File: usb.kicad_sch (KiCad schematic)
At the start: 46 parts, among them U10 CH397A, U11 XC6206PxxxMR, U3 XC6206PxxxMR, U4 CH343P, U6 CH334P, U9 CH343P, Y2 25MHz, Y3 12MHz

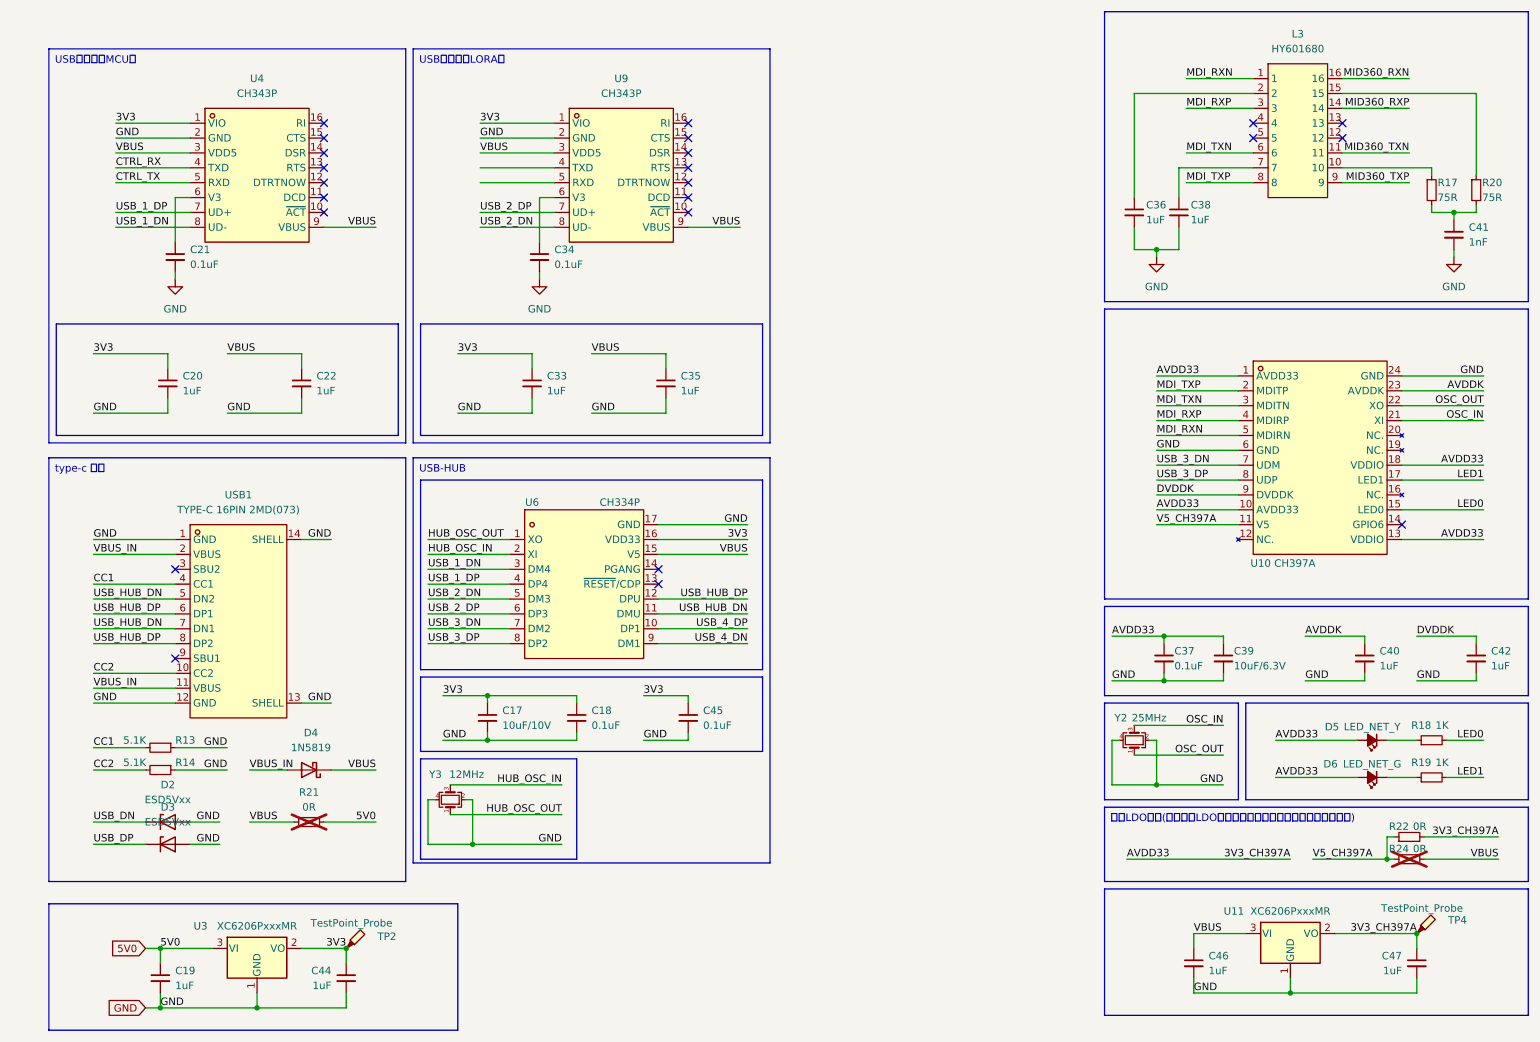
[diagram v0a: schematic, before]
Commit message: 暂存: 基本完成原理图(未分配封装，未ERC)
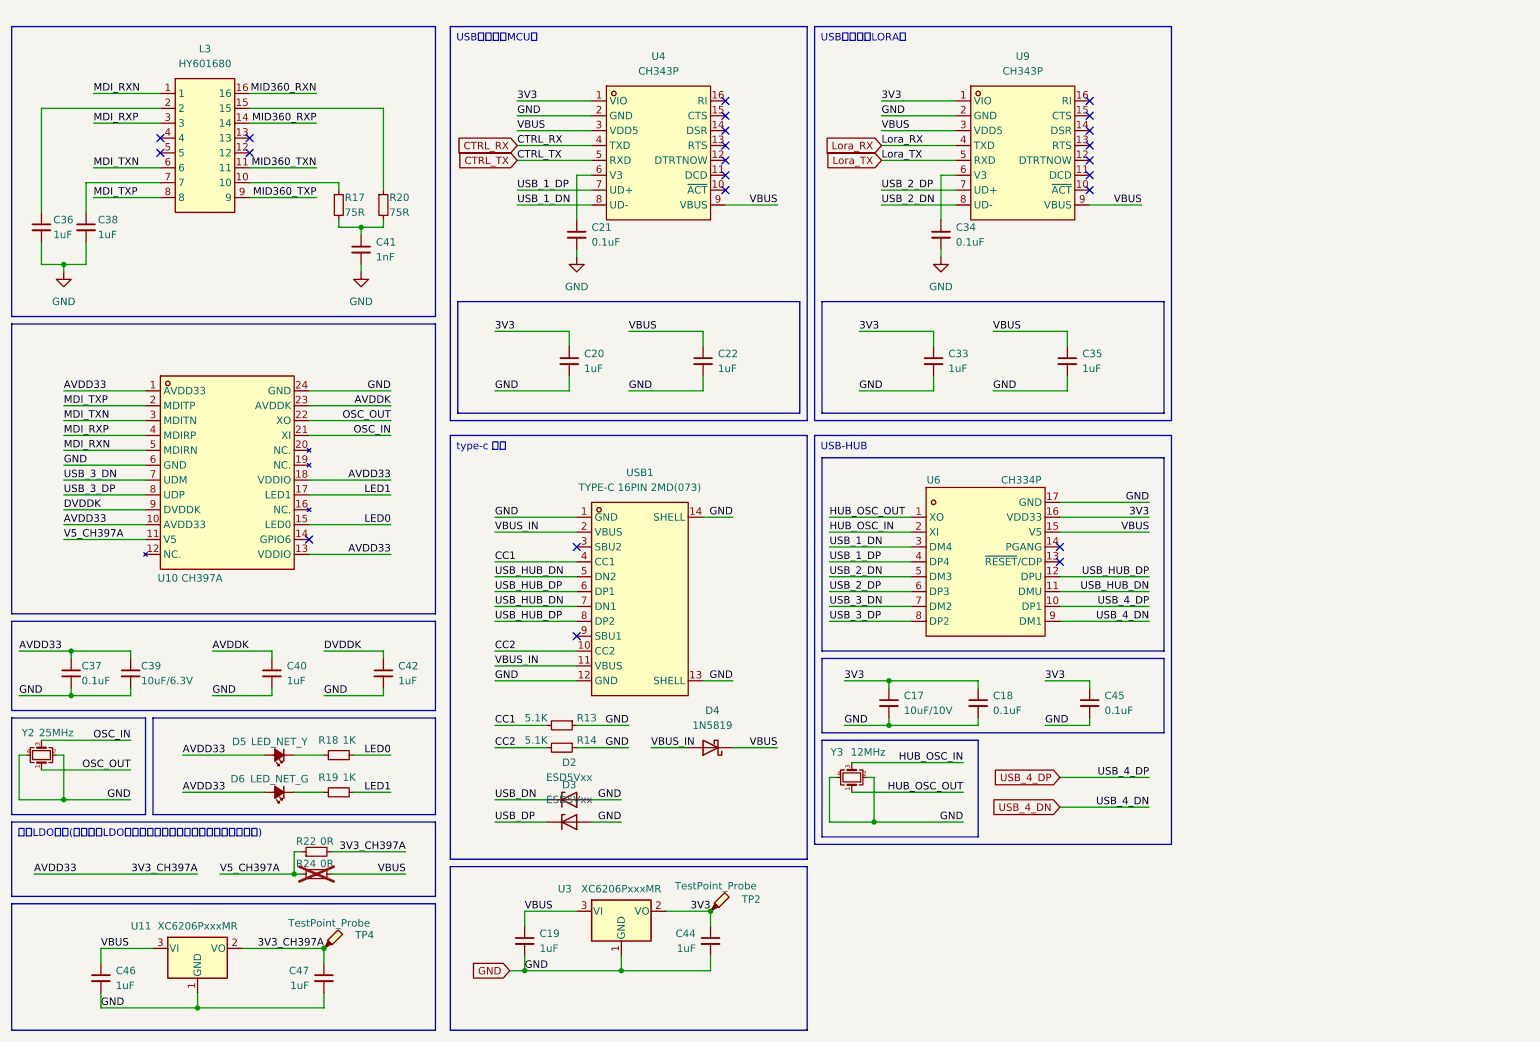
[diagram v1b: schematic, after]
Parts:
- removed R21: 0R, symbol Device:R_Small
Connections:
- net 5V0 is gone; now on net VBUS: C19.1, U3.3 (VI)
- net Lora_RX: now reaches U9.4 (TXD)
- net Lora_TX: now reaches U9.5 (RXD)
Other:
- moved on the sheet: C17, C18, C19, C20, C21, C22, C33, C34, C35, C36, C37, C38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

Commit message: 暂存: 基本完成原理图(差雷达接口)
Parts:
- C29: renamed from C36; footprint Capacitor_SMD:C_0603_1608Metric -> Capacitor_SMD:C_0402_1005Metric
- C32: renamed from C46; footprint Capacitor_SMD:C_0603_1608Metric -> Capacitor_SMD:C_0402_1005Metric
- C34: renamed from C40; footprint Capacitor_SMD:C_0603_1608Metric -> Capacitor_SMD:C_0402_1005Metric
- C35: renamed from C47; footprint Capacitor_SMD:C_0603_1608Metric -> Capacitor_SMD:C_0402_1005Metric
- C37: renamed from C42; footprint Capacitor_SMD:C_0603_1608Metric -> Capacitor_SMD:C_0402_1005Metric
- C38: renamed from C19; footprint Capacitor_SMD:C_0603_1608Metric -> Capacitor_SMD:C_0402_1005Metric
- C42: renamed from C44; footprint Capacitor_SMD:C_0603_1608Metric -> Capacitor_SMD:C_0402_1005Metric
- C43: renamed from C17; footprint (none) -> Capacitor_SMD:C_0402_1005Metric
- C46: renamed from C18; footprint (none) -> Capacitor_SMD:C_0402_1005Metric
- C48: renamed from C45; footprint (none) -> Capacitor_SMD:C_0402_1005Metric
- D2: renamed from D5; footprint LED_SMD:LED_0603_1608Metric -> LED_SMD:LED_0402_1005Metric
- D3: renamed from D6; footprint LED_SMD:LED_0603_1608Metric -> LED_SMD:LED_0402_1005Metric
- D6: renamed from D4; footprint Diode_THT:D_DO-41_SOD81_P10.16mm_Horizontal -> Diode_SMD:D_SOD-323
- R14: renamed from R22; footprint (none) -> Resistor_SMD:R_0402_1005Metric
- R15: renamed from R24; footprint (none) -> Resistor_SMD:R_0402_1005Metric
- renumbered C37 to C30, C38 to C31, C39 to C33, C41 to C36, C20 to C39, C21 to C40, C22 to C41, C33 to C44, C34 to C45, C35 to C47, D2 to D4, D3 to D5, R17 to R16, R18 to R17, R19 to R18, R20 to R19, R13 to R20, R14 to R21, TP4 to TP2, TP2 to TP3, U6 to U10, U9 to U11, U11 to U6, U10 to U7, U3 to U8, U4 to U9

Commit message: 暂存: 布局布线基本完成(DRC未过，GND不全)
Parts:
- renumbered C29 to C28, C30 to C29, C31 to C30, C32 to C31, C33 to C32, C34 to C33, C35 to C34, C36 to C35, C37 to C36, C38 to C37, C39 to C38, C40 to C39, C41 to C40, C42 to C41, C43 to C42, C44 to C43, C45 to C44, C46 to C45, C47 to C46, C48 to C47
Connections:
- net USB_DN is gone; now on net USB_HUB_DN: D4.1 (K)
- net USB_DP is gone; now on net USB_HUB_DP: D5.1 (K)
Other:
- moved on the sheet: D4, D5

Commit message: pref: USB外设改自供电，优化布线
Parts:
- removed D6: 1N5819, Diode_SMD:D_SOD-323, symbol Diode:1N5819
- R20, R21: value 5.1K -> 56K
- renumbered C28 to C32, C29 to C33, C30 to C34, C31 to C35, C32 to C36, C33 to C37, C34 to C38, C35 to C39, C36 to C40, C37 to C41, C38 to C42, C39 to C43, C40 to C44, C41 to C45, C42 to C46, C43 to C47, C44 to C48, C45 to C49, C46 to C50, C47 to C51
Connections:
- net VBUS_IN is gone; now on net VBUS: USB1.11 (VBUS), USB1.2 (VBUS)
- net EP: no longer R20.1, R21.1
- net USB_2_DN: now also U7.7 (UDM); no longer U11.8 (UD-)
- net USB_2_DP: now also U7.8 (UDP); no longer U11.7 (UD+)
- net USB_3_DN: now also U11.8 (UD-); no longer U7.7 (UDM)
- net USB_3_DP: now also U11.7 (UD+); no longer U7.8 (UDP)
- net VBUS: now also R20.1, R21.1; no longer C35.1, C41.1, C44.1, C50.1, R15.2, U10.15 (V5), U11.3 (VDD5), U11.9 (VBUS), U6.3 (VI), U8.3 (VI), U9.3 (VDD5), U9.9 (VBUS)
- new net 5V0_{assist}: C35.1, C41.1, C44.1, C50.1, R15.2, U10.15 (V5), U11.3 (VDD5), U11.9 (VBUS), U6.3 (VI), U8.3 (VI), U9.3 (VDD5), U9.9 (VBUS)
